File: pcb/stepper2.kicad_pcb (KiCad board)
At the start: 2 copper layers, 92 x 138 mm, 61 parts, among them J1 DA15_Receptacle_MountingHoles, J10 Conn_01x07_Pin, J11 FAN, J12 Conn_01x03_Pin, J13 Conn_01x03_Pin, J14 Conn_01x03_Pin, J2 DA15_Receptacle_MountingHoles, J3 DA15_Receptacle_MountingHoles, J4 DE15_Receptacle_HighDensity, J5 DE15_Receptacle_HighDensity, J6 DE15_Receptacle_HighDensity, J7 Conn_01x04_Pin, J8 Conn_01x05_Pin, J9 Conn_01x06_Pin, SW1 SW_Push, SW2 SW_Push, SW3 SW_Push, SW4 SW_Push, SW5 SW_Push, SW6 SW_Push, U1 AM26LS32ACN, U2 AM26LS32Ax, U3 AM26LS32ACN, U4 TMC2209_BIGTREETECH, U5 TMC2209_BIGTREETECH, U6 TMC2209_BIGTREETECH

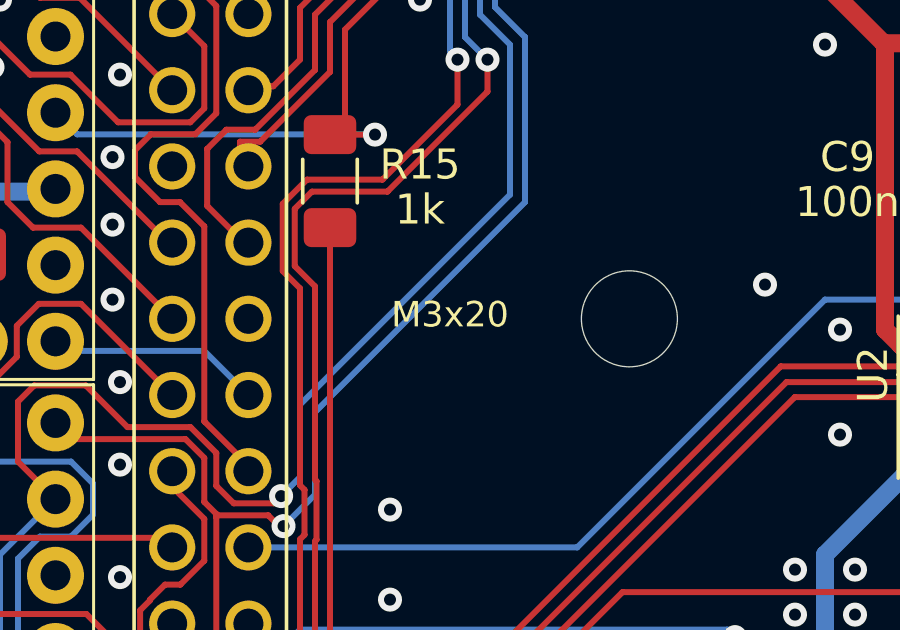
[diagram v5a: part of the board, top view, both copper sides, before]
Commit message: optimizations in PCB layout made in sync with the design of the case
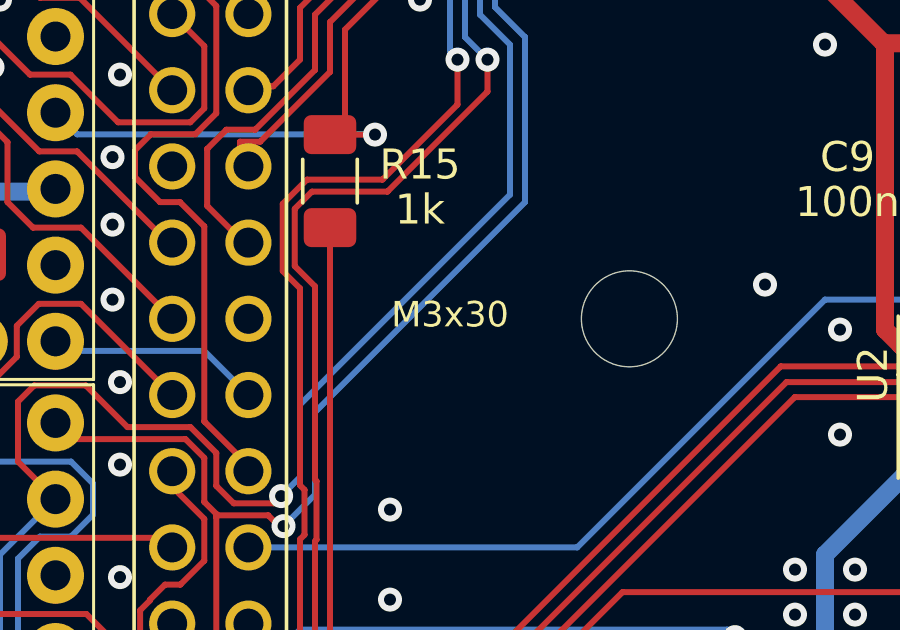
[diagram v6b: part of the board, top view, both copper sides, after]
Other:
- board text removed: "M3x20"
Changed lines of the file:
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@@
     (effects (font (size 0.85 0.85) (thickness 0.15) bold) (justify left bottom))
   )
-  (gr_text "M3x20" (at 41 -81) (layer "F.SilkS")
+  (gr_text "M3x30" (at 41 -81) (layer "F.SilkS")
     (effects (font (size 0.85 0.85) (thickness 0.15)))
   )
